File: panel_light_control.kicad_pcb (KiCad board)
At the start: 4 copper layers, 90 x 100 mm, 155 parts, among them J1 Conn_01x02, J11 RJ45_Shielded, J13 HR911105A, J2 RJ45_Shielded, J6 Conn_01x04, Q1 IRF540N, Q2 IRF540N, Q3 IRF540N, U1 L7805, U2 LM324, U3 STM32F207VGT6, U4 MCP2562-E-P, U5 LAN8720A, Y1 Crystal_GND24

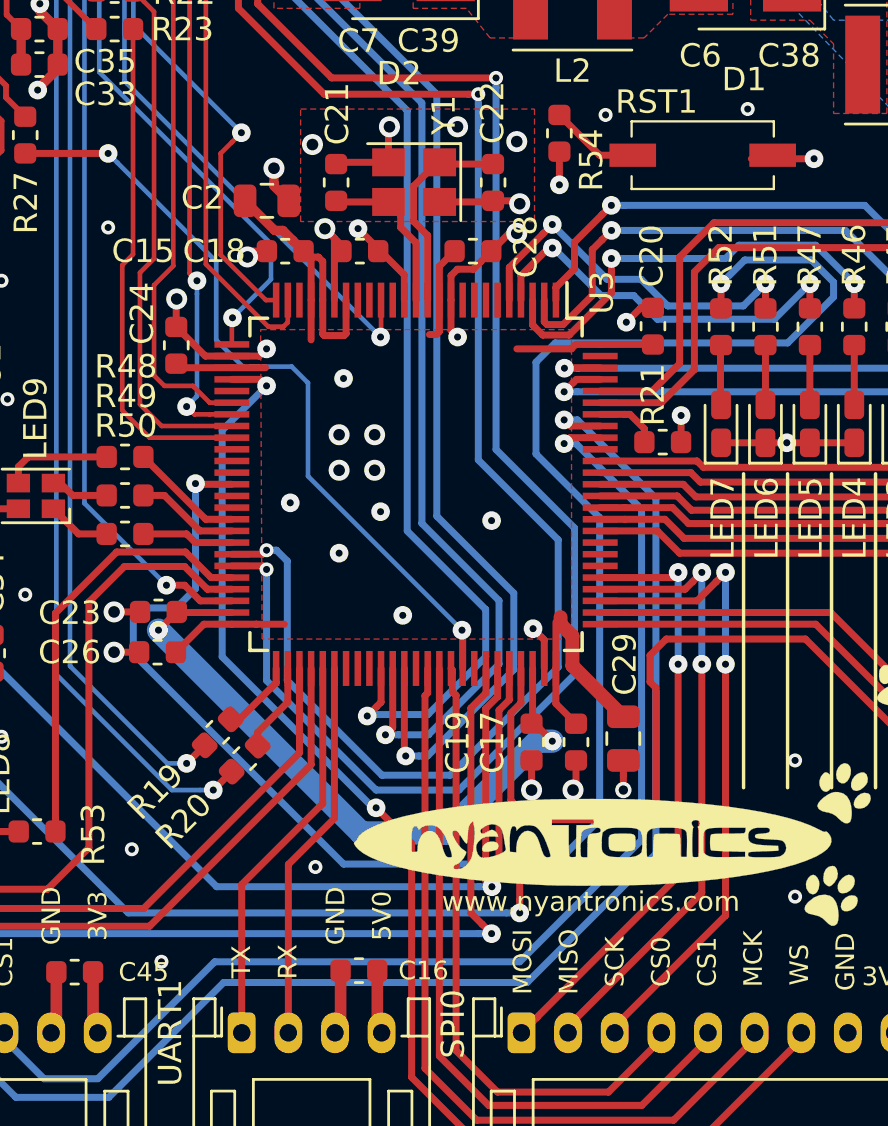
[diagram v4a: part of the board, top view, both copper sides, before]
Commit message: pinout validated against CubeMX listing (.ioc added), some nets renamed, system RGB LED reconnected. Reconnected I2C lines to include CAN alternate function. Warning: * bottom silkscreen labels might be invalidated
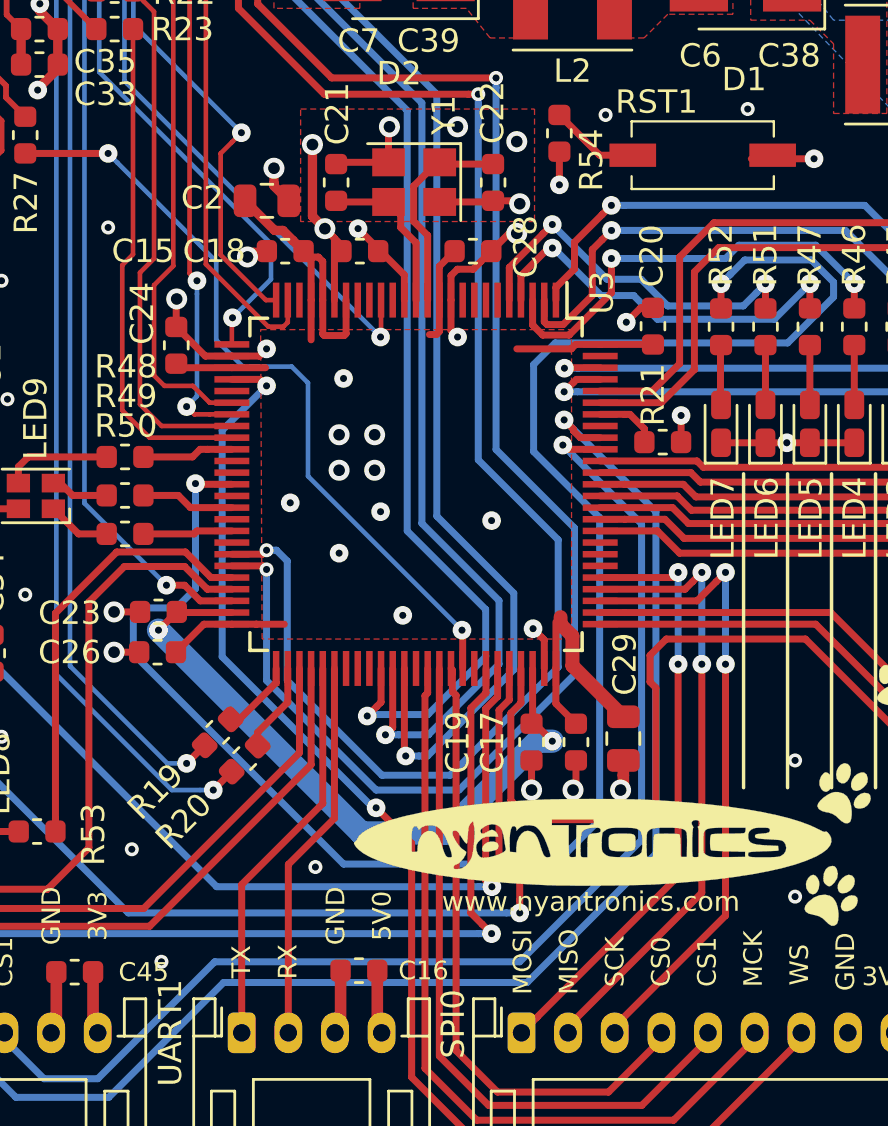
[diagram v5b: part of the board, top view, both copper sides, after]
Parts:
- R21: value 47k -> 1k
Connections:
- net LAN_RST renamed PHY_RST
- net PHY_VDDA renamed PYH_VDDA
- U3 pad 35: Net-(U3-Pad35) -> LED_SYSTEM_B
- U3 pad 40: Net-(U3-Pad40) -> LED_SYSTEM_G
- U3 pad 41: LED_SYSTEM_B -> Net-(U3-Pad41)
- U3 pad 42: LED_SYSTEM_G -> LED_SYSTEM_R
- U3 pad 43: LED_SYSTEM_R -> Net-(U3-Pad43)
- U3 pad 91: Net-(U3-Pad91) -> SPI1_CS1
- U3 pad 92: SPI1_CS1 -> SPI1_CS0
- U3 pad 93: SPI1_CS0 -> Net-(U3-Pad93)
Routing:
- net GND: track 125.5 -> 129.3 mm
- net LED_SYSTEM_B: track 4.90 -> 3.93 mm

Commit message: swap xtal for 12 MHz type with CL=8pF -> 2MHz PLL in (optimum), larger load capacitors offering higher noise immunity, HSE gain margin should still be ok, silk screen changes due to secondary CAN interface mapping to CS0+CS1 pins, system LED reconnected to TIM1+TIM3 PWM channels for ease of use. Migrated LAN8720A to pin / alternate function compatible LAN8742A. Details see migration guide http://ww1.microchip.com/downloads/en/AppNotes/en562713.pdf. Schematic and layout validation done. Note SPI0 and SPI1 refer to SPI2 and SPI3 peripherals... we'll have to see how much of an annoyance this turns out to be :) [this version is released to production]
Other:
- board text added: "PB5:SPI1_CS1"
- board text added: "PB6:SPI1_CS0"
- board text removed: "PB6:SPI1_CS1"
- board text removed: "PB7:SPI1_CS0"
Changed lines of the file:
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@@
     (31 B.Cu signal)
     (32 B.Adhes user)
-    (33 F.Adhes user)
-    (34 B.Paste user)
-    (35 F.Paste user)
+    (33 F.Adhes user hide)
+    (34 B.Paste user hide)
+    (35 F.Paste user hide)
     (36 B.SilkS user)
     (37 F.SilkS user)
@@
     (45 Margin user)
     (46 B.CrtYd user)
-    (47 F.CrtYd user)
+    (47 F.CrtYd user hide)
     (48 B.Fab user)
     (49 F.Fab user)
   )
   (setup
-    (last_trace_width 0.8)
+    (last_trace_width 0.2)
     (user_trace_width 0.2)
     (user_trace_width 0.25)
@@
     (effects (font (size 0.8 0.8) (thickness 0.15)) (justify mirror))
   )
-  (gr_text PB7:SPI1_CS0 (at 129.794 137.572667 90) (layer B.SilkS)
+  (gr_text PB6:SPI1_CS0 (at 129.794 137.572667 90) (layer B.SilkS)
     (effects (font (size 0.8 0.8) (thickness 0.15)) (justify mirror))
   )
@@
     (effects (font (size 0.8 0.8) (thickness 0.15)) (justify mirror))
   )
-  (gr_text PB6:SPI1_CS1 (at 131.826 137.572667 90) (layer B.SilkS)
+  (gr_text PB5:SPI1_CS1 (at 131.826 137.572667 90) (layer B.SilkS)
     (effects (font (size 0.8 0.8) (thickness 0.15)) (justify mirror))
   )
@@
   (segment (start 141.986 104.394) (end 137.3505 99.7585) (width 0.2) (layer B.Cu) (net 81))
   (segment (start 137.3505 99.7585) (end 137.3505 94.239807) (width 0.2) (layer B.Cu) (net 81))
-  (via (at 130.683 90.36201) (size 0.8) (drill 0.3) (layers F.Cu B.Cu) (net 170))
-  (segment (start 129.4385 90.678) (end 130.36701 90.678) (width 0.25) (layer F.Cu) (net 170))
-  (segment (start 130.918 92.475) (end 131.209999 92.183001) (width 0.25) (layer F.Cu) (net 170))
-  (segment (start 131.209999 90.889009) (end 131.082999 90.762009) (width 0.25) (layer F.Cu) (net 170))
-  (segment (start 131.082999 90.762009) (end 130.683 90.36201) (width 0.25) (layer F.Cu) (net 170))
-  (segment (start 130.918 94.3389) (end 130.918 92.475) (width 0.25) (layer F.Cu) (net 170))
-  (segment (start 130.36701 90.678) (end 130.683 90.36201) (width 0.25) (layer F.Cu) (net 170))
-  (segment (start 131.209999 92.183001) (end 131.209999 90.889009) (width 0.25) (layer F.Cu) (net 170))
-  (via (at 141.605 112.3315) (size 0.8) (drill 0.3) (layers F.Cu B.Cu) (net 170))
-  (segment (start 141.57646 113.47398) (end 141.57646 112.36004) (width 0.2) (layer F.Cu) (net 170))
-  (segment (start 141.57646 112.36004) (end 141.605 112.3315) (width 0.2) (layer F.Cu) (net 170))
-  (segment (start 141.605 112.3315) (end 143.256 110.6805) (width 0.2) (layer B.Cu) (net 170))
-  (segment (start 143.256 110.6805) (end 143.256 109.1565) (width 0.2) (layer B.Cu) (net 170))
-  (segment (start 143.256 109.1565) (end 135.89 101.7905) (width 0.2) (layer B.Cu) (net 170))
-  (segment (start 131.3815 91.06051) (end 131.082999 90.762009) (width 0.2) (layer B.Cu) (net 170))
-  (segment (start 131.3815 92.456) (end 131.3815 91.06051) (width 0.2) (layer B.Cu) (net 170))
-  (segment (start 131.666489 92.740989) (end 131.3815 92.456) (width 0.2) (layer B.Cu) (net 170))
-  (segment (start 131.082999 90.762009) (end 130.683 90.36201) (width 0.2) (layer B.Cu) (net 170))
-  (segment (start 135.89 96.012) (end 132.618989 92.740989) (width 0.2) (layer B.Cu) (net 170))
-  (segment (start 132.618989 92.740989) (end 131.666489 92.740989) (width 0.2) (layer B.Cu) (net 170))
-  (segment (start 135.89 101.7905) (end 135.89 96.012) (width 0.2) (layer B.Cu) (net 170))
   (segment (start 127.457 104.318) (end 126.289 104.318) (width 0.3) (layer F.Cu) (net 82) (status 20))
   (segment (start 129.032 102.819) (end 128.956 102.819) (width 0.3) (layer F.Cu) (net 82) (status 30))
@@
   (segment (start 120.0638 98.03638) (end 121.539 98.03638) (width 0.4) (layer F.Cu) (net 166))
   (segment (start 121.539 98.03638) (end 123.13138 98.03638) (width 0.4) (layer F.Cu) (net 166))
+  (via (at 130.683 90.36201) (size 0.8) (drill 0.3) (layers F.Cu B.Cu) (net 170))
+  (segment (start 129.4385 90.678) (end 130.36701 90.678) (width 0.25) (layer F.Cu) (net 170))
+  (segment (start 130.918 92.475) (end 131.209999 92.183001) (width 0.25) (layer F.Cu) (net 170))
+  (segment (start 131.209999 90.889009) (end 131.082999 90.762009) (width 0.25) (layer F.Cu) (net 170))
+  (segment (start 131.082999 90.762009) (end 130.683 90.36201) (width 0.25) (layer F.Cu) (net 170))
+  (segment (start 130.918 94.3389) (end 130.918 92.475) (width 0.25) (layer F.Cu) (net 170))
+  (segment (start 130.36701 90.678) (end 130.683 90.36201) (width 0.25) (layer F.Cu) (net 170))
+  (segment (start 131.209999 92.183001) (end 131.209999 90.889009) (width 0.25) (layer F.Cu) (net 170))
+  (via (at 141.605 112.3315) (size 0.8) (drill 0.3) (layers F.Cu B.Cu) (net 170))
+  (segment (start 141.57646 113.47398) (end 141.57646 112.36004) (width 0.2) (layer F.Cu) (net 170))
+  (segment (start 141.57646 112.36004) (end 141.605 112.3315) (width 0.2) (layer F.Cu) (net 170))
+  (segment (start 141.605 112.3315) (end 143.256 110.6805) (width 0.2) (layer B.Cu) (net 170))
+  (segment (start 143.256 110.6805) (end 143.256 109.1565) (width 0.2) (layer B.Cu) (net 170))
+  (segment (start 143.256 109.1565) (end 135.89 101.7905) (width 0.2) (layer B.Cu) (net 170))
+  (segment (start 131.3815 91.06051) (end 131.082999 90.762009) (width 0.2) (layer B.Cu) (net 170))
+  (segment (start 131.3815 92.456) (end 131.3815 91.06051) (width 0.2) (layer B.Cu) (net 170))
+  (segment (start 131.666489 92.740989) (end 131.3815 92.456) (width 0.2) (layer B.Cu) (net 170))
+  (segment (start 131.082999 90.762009) (end 130.683 90.36201) (width 0.2) (layer B.Cu) (net 170))
+  (segment (start 135.89 96.012) (end 132.618989 92.740989) (width 0.2) (layer B.Cu) (net 170))
+  (segment (start 132.618989 92.740989) (end 131.666489 92.740989) (width 0.2) (layer B.Cu) (net 170))
+  (segment (start 135.89 101.7905) (end 135.89 96.012) (width 0.2) (layer B.Cu) (net 170))
   (zone (net 2) (net_name GND) (layer F.Cu) (hatch edge 0.508)
     (priority 10)

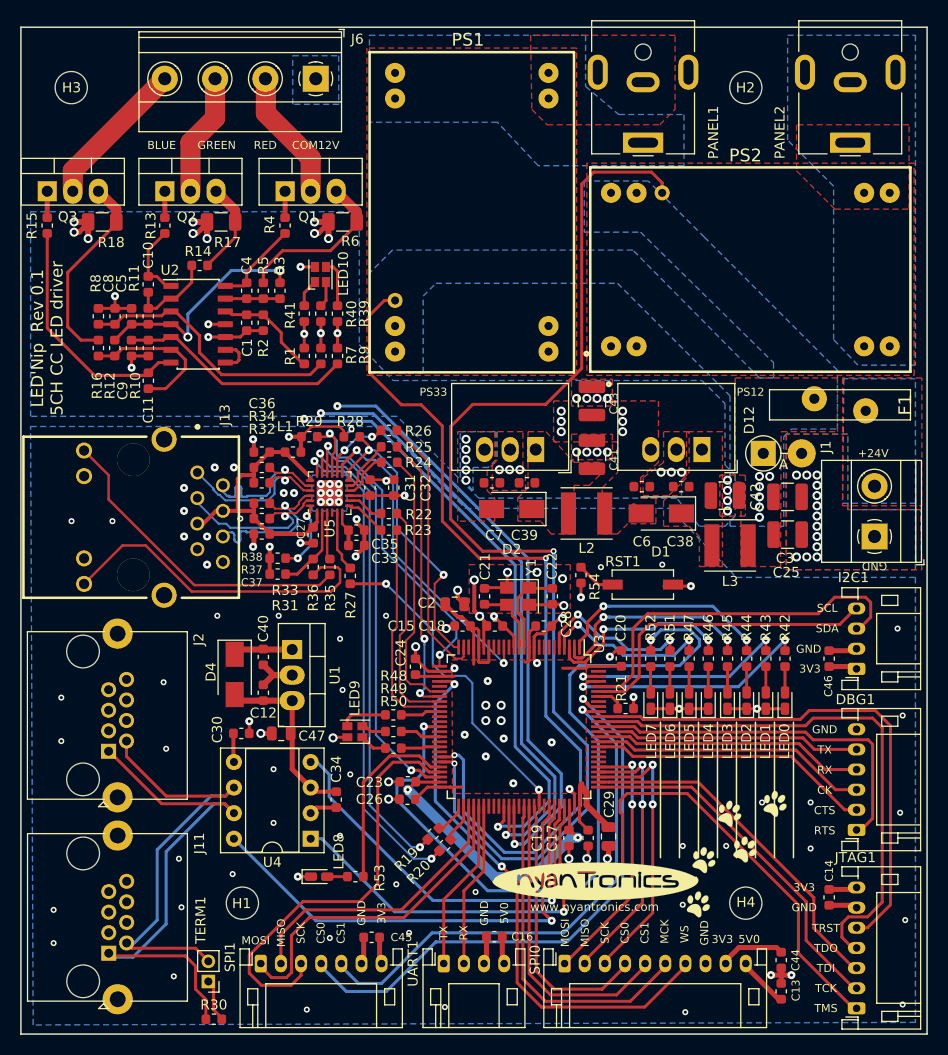
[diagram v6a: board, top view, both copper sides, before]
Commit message: final touches: add fiducials for PCBA
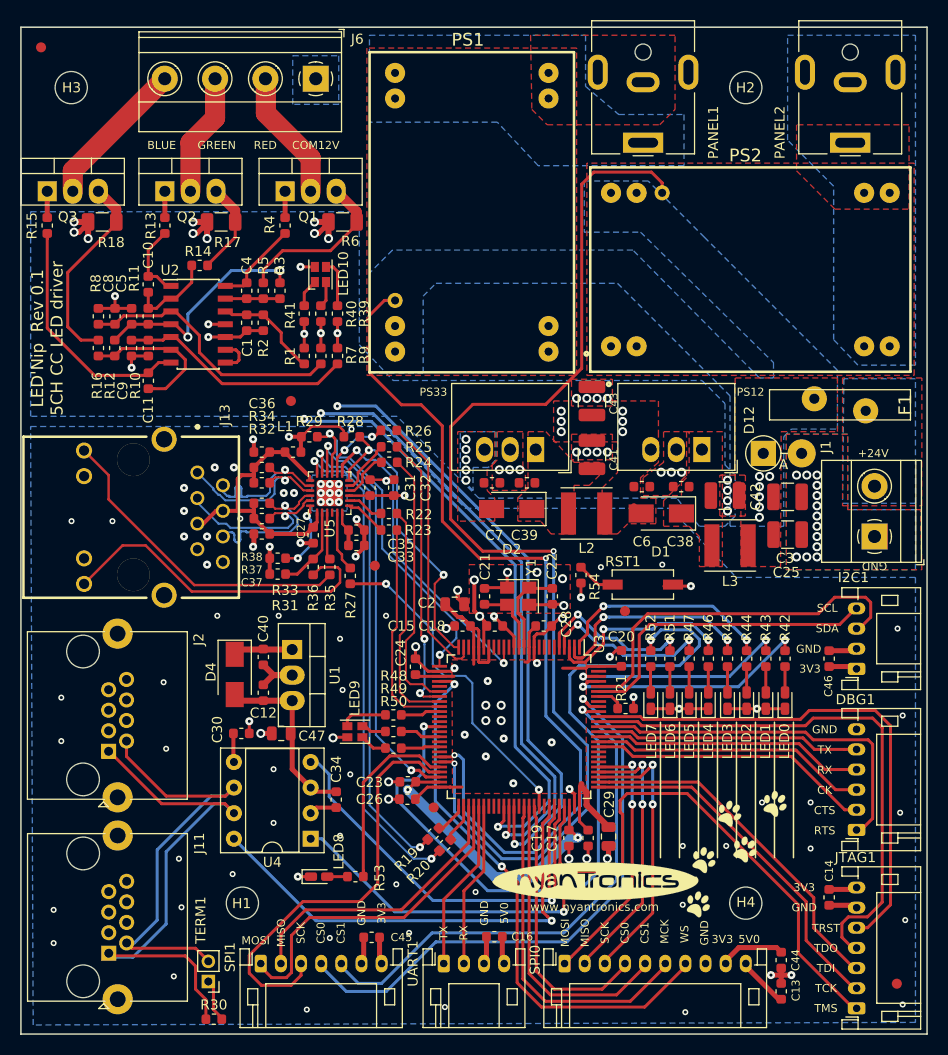
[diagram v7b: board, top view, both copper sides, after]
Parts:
- added FID1: Fiducial, Fiducial:Fiducial_1mm_Dia_2.54mm_Outer_CopperTop, F.Cu at (187.0, 145.0)
- added FID2: Fiducial, Fiducial:Fiducial_1mm_Dia_2.54mm_Outer_CopperTop, F.Cu at (141.1, 127.5)
- added FID3: Fiducial, Fiducial:Fiducial_1mm_Dia_2.54mm_Outer_CopperTop, F.Cu at (159.8, 108.4)
- added FID4: Fiducial, Fiducial:Fiducial_1mm_Dia_2.54mm_Outer_CopperTop, F.Cu at (135.2, 103.5)
- added FID5: Fiducial, Fiducial:Fiducial_1mm_Dia_2.54mm_Outer_CopperTop, F.Cu at (126.8, 87.1)
- added FID6: Fiducial, Fiducial:Fiducial_1mm_Dia_2.54mm_Outer_CopperTop, F.Cu at (102.0, 52.0)
- C21, C22: value 3pF -> 11pF
- U5: value LAN8720A -> LAN8742A
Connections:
- net RMII_RXER renamed PHY_AD0
